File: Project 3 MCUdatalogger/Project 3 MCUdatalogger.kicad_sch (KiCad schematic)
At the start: 1 part

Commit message: Setup of EEschema for new project
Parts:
- removed R1: R_US, symbol Device:R_US
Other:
- title: MCU Datalogger -> ${project_name}
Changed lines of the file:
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@@
 	(paper "A4")
 	(title_block
-		(title "MCU Datalogger")
+		(title "${project_name}")
 		(date "2024-11-26")
 		(rev "1")
 		(comment 1 "Author: Carlos Cortes")
 	)
-	(symbol
-		(lib_id "Device:R_US")
-		(at 57.15 79.375 0)
-		(unit 1)
-		(exclude_from_sim no)
-		(in_bom yes)
-		(on_board yes)
-		(dnp no)
-		(fields_autoplaced yes)
-		(property "Reference" "R1"
-			(at 59.69 78.1049 0)
-			(effects
-				(font
-					(size 1.27 1.27)
-				)
-				(justify left)
-			)
-		)
-		(property "Value" "R_US"
-			(at 59.69 80.6449 0)
-			(effects
-				(font
-					(size 1.27 1.27)
-				)
-				(justify left)
-			)
-		)
-		(property "Footprint" ""
-			(at 58.166 79.629 90)
-			(effects
-				(font
-					(size 1.27 1.27)
-				)
-				(hide yes)
-			)
-		)
-		(property "Datasheet" "~"
-			(at 57.15 79.375 0)
-			(effects
-				(font
-					(size 1.27 1.27)
-				)
-				(hide yes)
-			)
-		)
-		(property "Description" "Resistor, US symbol"
-			(at 57.15 79.375 0)
-			(effects
-				(font
-					(size 1.27 1.27)
-				)
-				(hide yes)
-			)
-		)
-		(pin "1"
-		)
-		(pin "2"
-		)
-		(instances
-			(project ""
-				(path "/7d5d1e2c-b308-4025-bcdd-7450c663d83b"
-					(reference "R1")
-					(unit 1)
-				)
-			)
-		)
-	)
 	(sheet_instances

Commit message: Have added the required symbols to the schematic sheets
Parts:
- added BT1: Battery, symbol Device:Battery
- added C1, C2, C3, C4: C, symbol Device:C
- added C5: C_Polarized_US, symbol Device:C_Polarized_US
- added D1, D2: LED, symbol Device:LED
- added H1, H2, H3, H4: MountingHole, symbol Mechanical:MountingHole
- added R1, R2, R3, R4, R5, R6, R7: R_US, symbol Device:R_US
- added U1, U2: 24LC1025, symbol Memory_EEPROM:24LC1025
- added U3: ATMEGA328P-AU, ATMEGA328P-AU:QFP80P900X900X120-32N, symbol ATMEGA328P-AU:ATMEGA328P-AU
- added U4: DS1337S_, DS1337S_:SOIC127P600X175-8N, symbol DS1337S_:DS1337S_
- added Y1, Y2: Crystal, symbol Device:Crystal
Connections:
- new net: U3.21 (GND), U3.3 (GND), U3.5 (GND)
- new net: U3.4 (VCC), U3.6 (VCC)
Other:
- added sheet Connectors (connectors.kicad_sch)

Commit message: Change locations of symbols (arrange).
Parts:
- renumbered C4 to C1, C1 to C4, D2 to D1, D1 to D2, R3 to R1, R4 to R2, R5 to R3, R6 to R4, R2 to R5, R7 to R6, R1 to R7, U4 to U2, U2 to U3, U3 to U4
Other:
- moved on the sheet: BT1, C1, C2, C3, C4, C5, D1, D2, H1, H2, H3, H4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

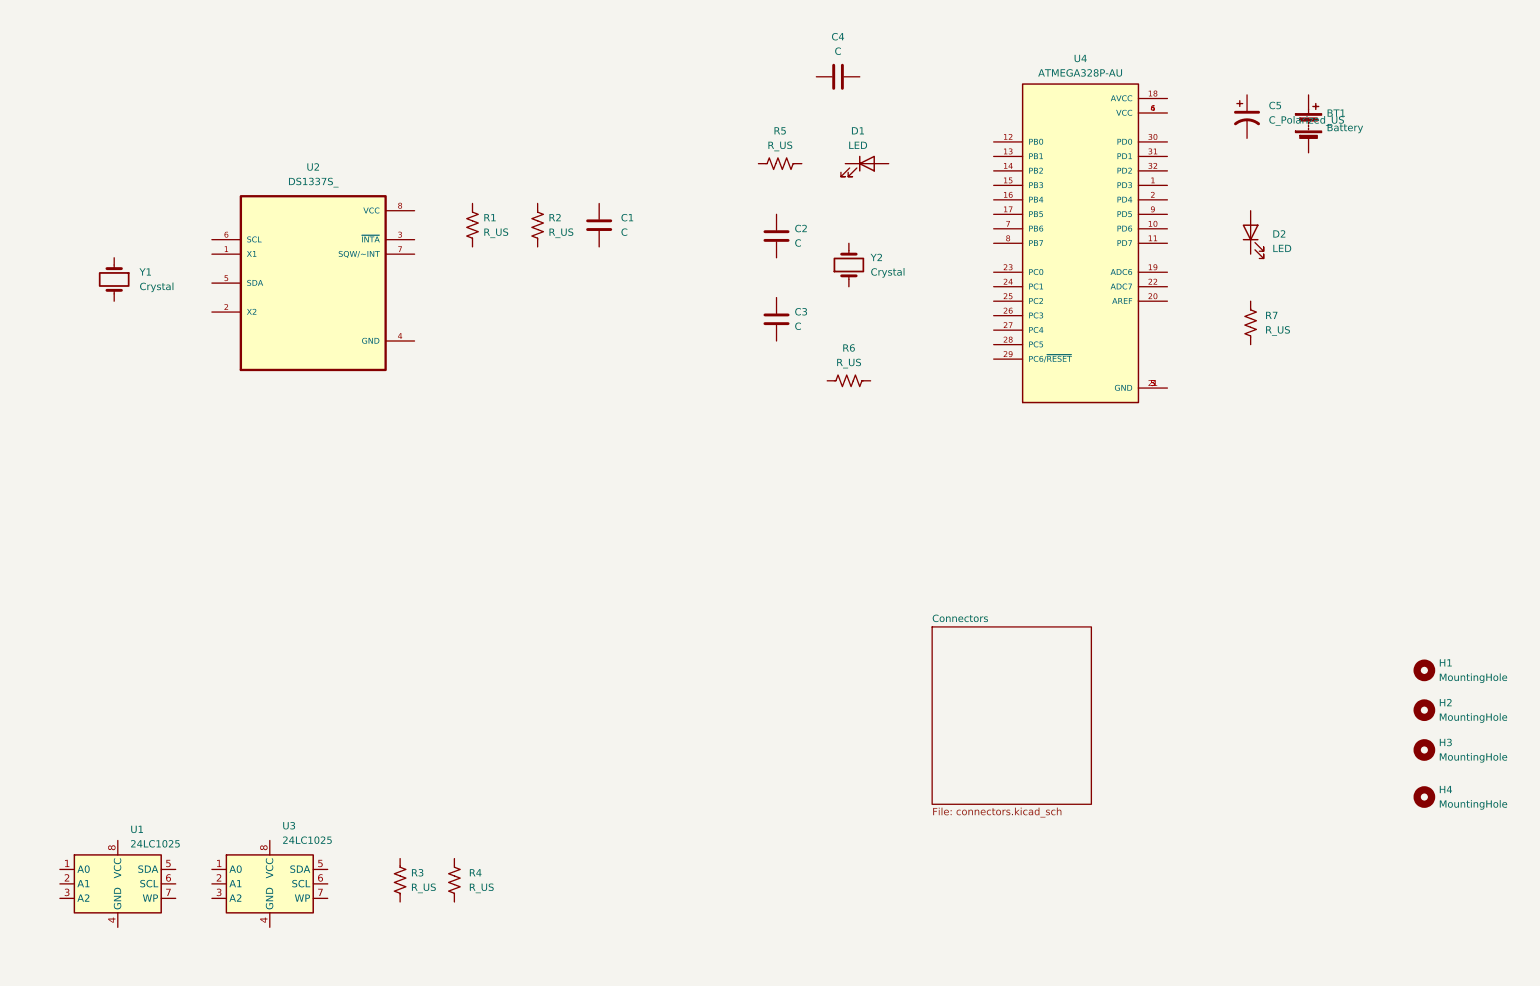
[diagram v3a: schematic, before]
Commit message: Added component values
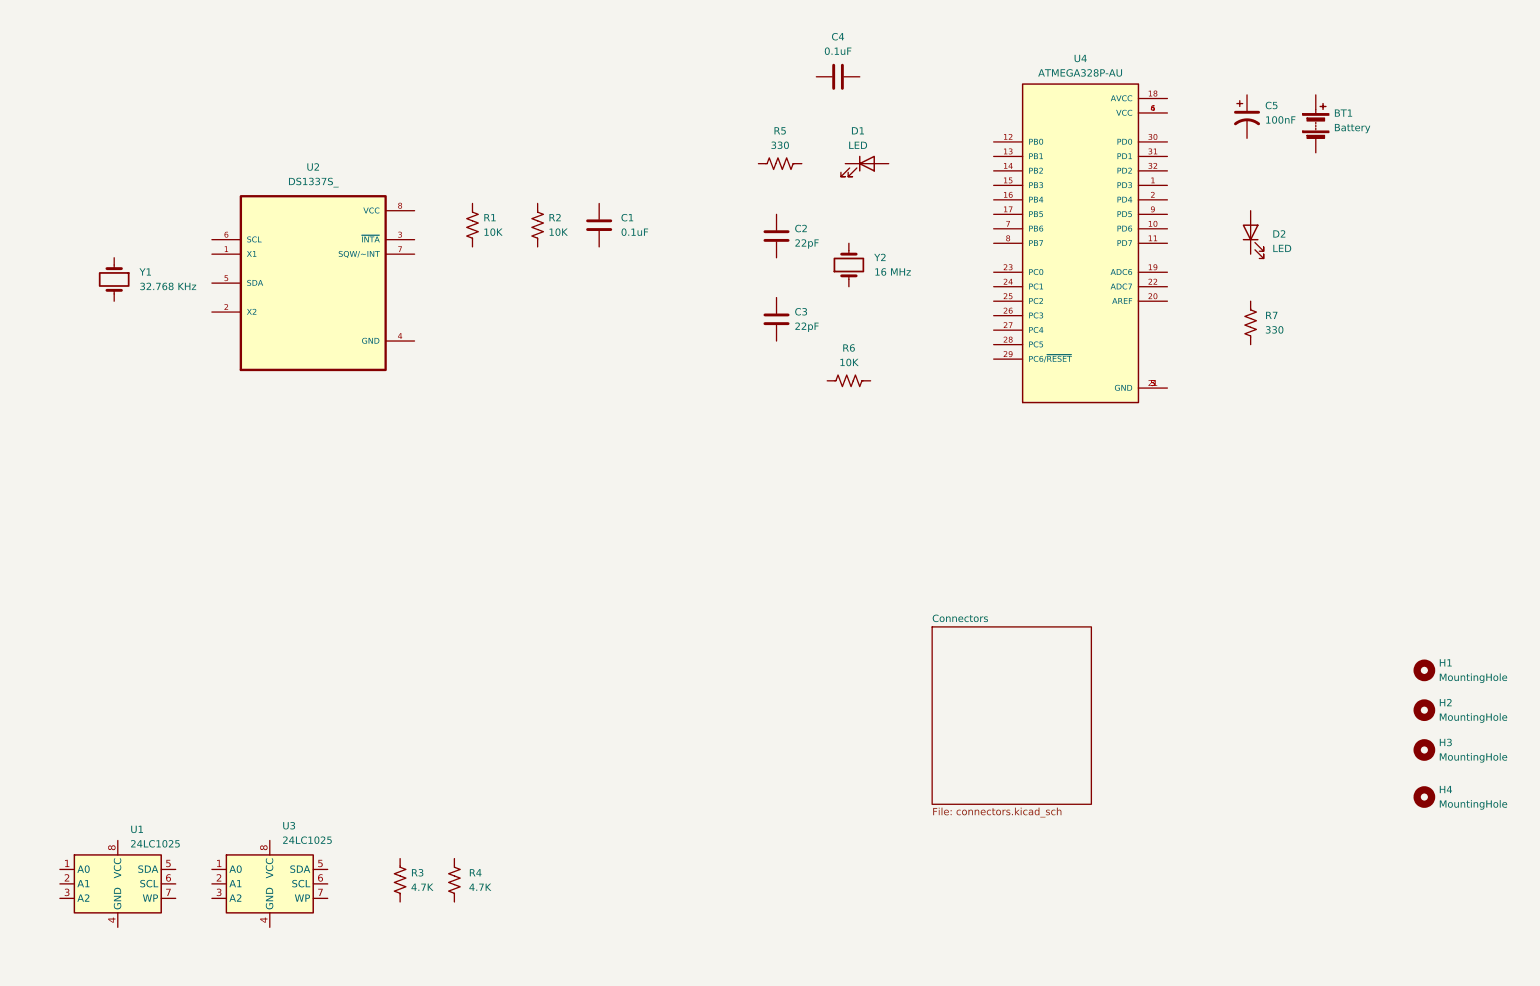
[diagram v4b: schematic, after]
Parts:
- C1, C4: value C -> 0.1uF
- C2, C3: value C -> 22pF
- C5: value C_Polarized_US -> 100nF
- R1, R2, R6: value R_US -> 10K
- R3, R4: value R_US -> 4.7K
- R5, R7: value R_US -> 330
- Y1: value Crystal -> 32.768 KHz
- Y2: value Crystal -> 16 MHz
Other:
- moved on the sheet: BT1
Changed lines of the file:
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@@
 		(fields_autoplaced yes)
 		(property "Reference" "C5"
-			(at 236.855 40.0049 0)
-			(effects
-				(font
-					(size 1.27 1.27)
-				)
-				(justify left)
-			)
-		)
-		(property "Value" "C_Polarized_US"
-			(at 236.855 42.5449 0)
+			(at 236.22 40.0049 0)
+			(effects
+				(font
+					(size 1.27 1.27)
+				)
+				(justify left)
+			)
+		)
+		(property "Value" "100nF"
+			(at 236.22 42.5449 0)
 			(effects
 				(font
@@
 			)
 		)
-		(property "Value" "C"
+		(property "Value" "22pF"
 			(at 153.67 78.7399 0)
 			(effects
@@
 			)
 		)
-		(property "Value" "R_US"
+		(property "Value" "10K"
 			(at 99.06 62.2299 0)
 			(effects
@@
 			)
 		)
-		(property "Value" "C"
+		(property "Value" "0.1uF"
 			(at 161.29 30.48 90)
 			(effects
@@
 			)
 		)
-		(property "Value" "C"
+		(property "Value" "0.1uF"
 			(at 123.19 62.2299 0)
 			(effects
@@
 			)
 		)
-		(property "Value" "R_US"
+		(property "Value" "330"
 			(at 236.22 79.3749 0)
 			(effects
@@
 		(fields_autoplaced yes)
 		(property "Reference" "Y2"
-			(at 167.005 66.6749 90)
+			(at 167.64 66.6749 90)
 			(effects
 				(font
@@
 			)
 		)
-		(property "Value" "Crystal"
-			(at 167.005 69.2149 90)
+		(property "Value" "16 MHz"
+			(at 167.64 69.2149 90)
 			(effects
 				(font
@@
 			)
 		)
-		(property "Value" "R_US"
+		(property "Value" "10K"
 			(at 110.49 62.2299 0)
 			(effects
@@
 			)
 		)
-		(property "Value" "R_US"
+		(property "Value" "4.7K"
 			(at 86.36 177.1649 0)
 			(effects
@@
 			)
 		)
-		(property "Value" "Crystal"
+		(property "Value" "32.768 KHz"
 			(at 38.735 71.7549 90)
 			(effects
@@
 			)
 		)
+		(property "Purpose" ""
+			(at 34.29 70.485 0)
+			(effects
+				(font
+					(size 1.27 1.27)
+				)
+			)
+		)
 		(pin "1"
 		)
@@
 			)
 		)
-		(property "Value" "R_US"
+		(property "Value" "4.7K"
 			(at 96.52 177.1649 0)
 			(effects
@@
 			)
 		)
-		(property "Value" "R_US"
+		(property "Value" "10K"
 			(at 163.195 85.09 90)
 			(effects
@@
 			)
 		)
-		(property "Value" "R_US"
+		(property "Value" "330"
 			(at 151.13 46.99 90)
 			(effects
@@
 	(symbol
 		(lib_id "Device:Battery")
-		(at 243.84 43.18 0)
+		(at 245.11 43.18 0)
 		(unit 1)
 		(exclude_from_sim no)
@@
 		(fields_autoplaced yes)
 		(property "Reference" "BT1"
-			(at 247.015 41.3384 0)
+			(at 248.285 41.3384 0)
 			(effects
 				(font
@@
 		)
 		(property "Value" "Battery"
-			(at 247.015 43.8784 0)
-			(effects
-				(font
-					(size 1.27 1.27)
-				)
-				(justify left)
-			)
-		)
-		(property "Footprint" ""
-			(at 243.84 41.656 90)
-			(effects
-				(font
-					(size 1.27 1.27)
-				)
-				(hide yes)
-			)
-		)
-		(property "Datasheet" "~"
-			(at 243.84 41.656 90)
+			(at 248.285 43.8784 0)
+			(effects
+				(font
+					(size 1.27 1.27)
+				)
+				(justify left)
+			)
+		)
+		(property "Footprint" ""
+			(at 245.11 41.656 90)
+			(effects
+				(font
+					(size 1.27 1.27)
+				)
+				(hide yes)
+			)
+		)
+		(property "Datasheet" "~"
+			(at 245.11 41.656 90)
 			(effects
 				(font
@@
 		)
 		(property "Description" "Multiple-cell battery"
-			(at 243.84 43.18 0)
+			(at 245.11 43.18 0)
 			(effects
 				(font
@@
 			)
 		)
-		(property "Value" "C"
+		(property "Value" "22pF"
 			(at 153.67 64.1349 0)
 			(effects

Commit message: Completed Symbol to footprint associations
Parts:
- BT1: footprint (none) -> Connector_PinHeader_2.54mm:PinHeader_1x02_P2.54mm_Vertical
- C1, C2, C3, C4, C5: footprint (none) -> Capacitor_SMD:C_0805_2012Metric
- D1, D2: footprint (none) -> LED_SMD:LED_0805_2012Metric
- H1, H2, H3, H4: footprint (none) -> MountingHole:MountingHole_2.1mm
- R1, R2, R3, R4, R5, R6, R7: footprint (none) -> Resistor_SMD:R_0805_2012Metric
- U1, U3: footprint (none) -> Package_SO:SOIC-8_5.23x5.23mm_P1.27mm
- Y1, Y2: footprint (none) -> Crystal:Crystal_SMD_Abracon_ABM3-2Pin_5.0x3.2mm_HandSoldering
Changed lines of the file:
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@@
 			)
 		)
-		(property "Footprint" ""
+		(property "Footprint" "Capacitor_SMD:C_0805_2012Metric"
 			(at 233.045 41.91 0)
 			(effects
@@
 			)
 		)
-		(property "Footprint" ""
+		(property "Footprint" "LED_SMD:LED_0805_2012Metric"
 			(at 166.37 50.165 0)
 			(effects
@@
 			)
 		)
-		(property "Footprint" ""
+		(property "Footprint" "Capacitor_SMD:C_0805_2012Metric"
 			(at 151.4602 81.28 0)
 			(effects
@@
 			)
 		)
-		(property "Footprint" ""
+		(property "Footprint" "Resistor_SMD:R_0805_2012Metric"
 			(at 98.171 61.214 90)
 			(effects
@@
 			)
 		)
-		(property "Footprint" ""
+		(property "Footprint" "LED_SMD:LED_0805_2012Metric"
 			(at 233.68 62.23 0)
 			(effects
@@
 			)
 		)
-		(property "Footprint" ""
+		(property "Footprint" "Capacitor_SMD:C_0805_2012Metric"
 			(at 165.1 33.9598 0)
 			(effects
@@
 			)
 		)
-		(property "Footprint" ""
+		(property "Footprint" "Capacitor_SMD:C_0805_2012Metric"
 			(at 120.3452 64.77 0)
 			(effects
@@
 			)
 		)
-		(property "Footprint" ""
+		(property "Footprint" "Resistor_SMD:R_0805_2012Metric"
 			(at 234.696 78.359 90)
 			(effects
@@
 			)
 		)
-		(property "Footprint" ""
+		(property "Footprint" "Crystal:Crystal_SMD_Abracon_ABM3-2Pin_5.0x3.2mm_HandSoldering"
 			(at 163.195 67.945 0)
 			(effects
@@
 			)
 		)
-		(property "Footprint" ""
+		(property "Footprint" "MountingHole:MountingHole_2.1mm"
 			(at 264.16 139.065 0)
 			(effects
@@
 			)
 		)
-		(property "Footprint" ""
+		(property "Footprint" "MountingHole:MountingHole_2.1mm"
 			(at 264.16 146.05 0)
 			(effects
@@
 			)
 		)
-		(property "Footprint" ""
+		(property "Footprint" "Resistor_SMD:R_0805_2012Metric"
 			(at 109.601 61.214 90)
 			(effects
@@
 			)
 		)
-		(property "Footprint" ""
+		(property "Footprint" "Resistor_SMD:R_0805_2012Metric"
 			(at 85.471 176.149 90)
 			(effects
@@
 			)
 		)
-		(property "Footprint" ""
+		(property "Footprint" "Package_SO:SOIC-8_5.23x5.23mm_P1.27mm"
 			(at 34.925 176.53 0)
 			(effects
@@
 			)
 		)
-		(property "Footprint" ""
+		(property "Footprint" "Crystal:Crystal_SMD_Abracon_ABM3-2Pin_5.0x3.2mm_HandSoldering"
 			(at 34.29 70.485 0)
 			(effects
@@
 			)
 		)
-		(property "Footprint" ""
+		(property "Footprint" "MountingHole:MountingHole_2.1mm"
 			(at 264.16 161.29 0)
 			(effects
@@
 			)
 		)
-		(property "Footprint" ""
+		(property "Footprint" "Resistor_SMD:R_0805_2012Metric"
 			(at 94.996 176.149 90)
 			(effects
@@
 			)
 		)
-		(property "Footprint" ""
+		(property "Footprint" "Resistor_SMD:R_0805_2012Metric"
 			(at 163.449 87.249 90)
 			(effects
@@
 			)
 		)
-		(property "Footprint" ""
+		(property "Footprint" "Package_SO:SOIC-8_5.23x5.23mm_P1.27mm"
 			(at 61.595 176.53 0)
 			(effects
@@
 			)
 		)
-		(property "Footprint" ""
+		(property "Footprint" "Resistor_SMD:R_0805_2012Metric"
 			(at 151.384 49.149 90)
 			(effects
@@
 			)
 		)
-		(property "Footprint" ""
+		(property "Footprint" "Connector_PinHeader_2.54mm:PinHeader_1x02_P2.54mm_Vertical"
 			(at 245.11 41.656 90)
 			(effects
@@
 			)
 		)
-		(property "Footprint" ""
+		(property "Footprint" "MountingHole:MountingHole_2.1mm"
 			(at 264.16 153.035 0)
 			(effects
@@
 			)
 		)
-		(property "Footprint" ""
+		(property "Footprint" "Capacitor_SMD:C_0805_2012Metric"
 			(at 151.4602 66.675 0)
 			(effects
